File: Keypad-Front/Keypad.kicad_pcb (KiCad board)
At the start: 4 copper layers, 100.1 x 192.1 mm, 99 parts, among them J1 RTC STEMMA QT, J6 EXP QWIIC, J7 TOUCH QWIIC, U1 DS3231MZ, U2 PCA9536DP, U3 CAP1214, U4 PN5321A3HN_C1xx, U5 MCP9808_MSOP, Y3 27.12MHz

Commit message: Simplify schematic and PCB
Remove the solder jumper for SEL0/SEL1, that's been tested & is correct.

Add 0-ohm resistors for GPIO expander to accomodate future green wire hacks.

Mark the DNP components on the schematic.
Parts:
- removed JP1: SEL0, Jumper:SolderJumper-3_P1.3mm_Bridged12_Pad1.0x1.5mm
- removed JP2: SEL1, Jumper:SolderJumper-3_P1.3mm_Bridged12_Pad1.0x1.5mm
- added R31: 0, Resistor_SMD:R_0805_2012Metric_Pad1.20x1.40mm_HandSolder, B.Cu at (123.1, 181.0)
- added R32: 0, Resistor_SMD:R_0805_2012Metric_Pad1.20x1.40mm_HandSolder, B.Cu at (125.6, 181.0)
- added R33: 0, Resistor_SMD:R_0805_2012Metric_Pad1.20x1.40mm_HandSolder, B.Cu at (128.1, 181.0)
- BT1: value Battery_Cell -> CR2032
- C1, C4: value 0.1uF -> .1uF
- moved U2 0.62 mm to (123.8, 185.3)
- moved C27 0.31 mm to (124.5, 188.8)
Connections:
- U2 pad 2: GND1 -> Net-(U2-IO1)
- U2 pad 3: GND1 -> Net-(U2-IO2)
- U2 pad 5: GND1 -> Net-(U2-IO3)
- U4 pad 16: /SEL0 -> +3.3V
- U4 pad 17: /SEL1 -> GND1
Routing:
- net /SEL1: track 37.3 -> 0.00 mm, vias 2 -> 0
- net /SEL0: track 30.8 -> 0.00 mm, vias 2 -> 0
- net GND1: track 2636.9 -> 2608.6 mm, vias 40 -> 41
- net Net-(U2-IO2): track 0.00 -> 7.70 mm
- net Net-(U2-IO1): track 0.00 -> 7.02 mm
- net +3.3V: track 647.7 -> 653.9 mm
- net Net-(U2-IO3): track 0.00 -> 4.08 mm
- net /LED12: track 63.4 -> 65.0 mm
- net /TOUCH_SCL: track 273.8 -> 273.3 mm
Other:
- board text added: "CSA 2023-10-25"
- board text removed: "0"
- board text removed: "1"
- board text removed: "CSA 2023-09-27"

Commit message: More schematic cleanup
* Remove silkscreen for R23/R24, which are shorted jumpers as a netlist
hack for the PCB antenna, not "real" components.

* Remove unnecessary R15 (and its traces) now that we have PCA9536 to
drive LED12.
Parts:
- removed R15: 0, Resistor_SMD:R_0805_2012Metric_Pad1.20x1.40mm_HandSolder
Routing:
- net /LED10: track 83.2 -> 65.7 mm, vias 2 -> 0
- net /LED12: track 65.0 -> 62.8 mm
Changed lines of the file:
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@@
     (attr exclude_from_pos_files)
     (net_tie_pad_groups "1, 2")
-    (fp_text reference "R23" (at 0 -2) (layer "B.SilkS")
+    (fp_text reference "R23" (at 0 -2) (layer "B.SilkS") hide
         (effects (font (size 1 1) (thickness 0.15)) (justify mirror))
     )
@@
     (attr exclude_from_pos_files)
     (net_tie_pad_groups "1, 2")
-    (fp_text reference "R24" (at 0 -2) (layer "B.SilkS")
+    (fp_text reference "R24" (at 0 -2) (layer "B.SilkS") hide
         (effects (font (size 1 1) (thickness 0.15)) (justify mirror))
     )
@@
     )
   )
-  (footprint "Resistor_SMD:R_0805_2012Metric_Pad1.20x1.40mm_HandSolder" (layer "B.Cu")
-    (at 116.5625 185 90)
-    (descr "Resistor SMD 0805 (2012 Metric), square (rectangular) end terminal, IPC_7351 nominal with elongated pad for handsoldering. (Body size source: IPC-SM-782 page 72, https://www.pcb-3d.com/wordpress/wp-content/uploads/ipc-sm-782a_amendment_1_and_2.pdf), generated with kicad-footprint-generator")
-    (tags "resistor handsolder")
-    (property "Sheetfile" "Keypad.kicad_sch")
-    (property "Sheetname" "")
-    (property "dnp" "")
-    (property "ki_description" "Resistor, small US symbol")
-    (property "ki_keywords" "r resistor")
-    (attr smd)
-    (fp_text reference "R15" (at -3.125 0 180) (layer "B.SilkS")
-        (effects (font (size 1 1) (thickness 0.15)) (justify mirror))
-    )
-    (fp_text value "0" (at 0 -1.65 90) (layer "B.Fab")
-        (effects (font (size 1 1) (thickness 0.15)) (justify mirror))
-    )
-    (fp_text user "${REFERENCE}" (at 0 0 90) (layer "B.Fab")
-        (effects (font (size 0.5 0.5) (thickness 0.08)) (justify mirror))
-    )
-    (fp_line (start -0.227064 -0.735) (end 0.227064 -0.735)
-      (stroke (width 0.12) (type solid)) (layer "B.SilkS"))
-    (fp_line (start -0.227064 0.735) (end 0.227064 0.735)
-      (stroke (width 0.12) (type solid)) (layer "B.SilkS"))
-    (fp_line (start -1.85 -0.95) (end -1.85 0.95)
-      (stroke (width 0.05) (type solid)) (layer "B.CrtYd"))
-    (fp_line (start -1.85 0.95) (end 1.85 0.95)
-      (stroke (width 0.05) (type solid)) (layer "B.CrtYd"))
-    (fp_line (start 1.85 -0.95) (end -1.85 -0.95)
-      (stroke (width 0.05) (type solid)) (layer "B.CrtYd"))
-    (fp_line (start 1.85 0.95) (end 1.85 -0.95)
-      (stroke (width 0.05) (type solid)) (layer "B.CrtYd"))
-    (fp_line (start -1 -0.625) (end -1 0.625)
-      (stroke (width 0.1) (type solid)) (layer "B.Fab"))
-    (fp_line (start -1 0.625) (end 1 0.625)
-      (stroke (width 0.1) (type solid)) (layer "B.Fab"))
-    (fp_line (start 1 -0.625) (end -1 -0.625)
-      (stroke (width 0.1) (type solid)) (layer "B.Fab"))
-    (fp_line (start 1 0.625) (end 1 -0.625)
-      (stroke (width 0.1) (type solid)) (layer "B.Fab"))
-    (pad "1" smd roundrect (at -1 0 90) (size 1.2 1.4) (layers "B.Cu" "B.Paste" "B.Mask") (roundrect_rratio 0.2083333333)
-      (net 33 "/LED10") (pintype "passive"))
-    (pad "2" smd roundrect (at 1 0 90) (size 1.2 1.4) (layers "B.Cu" "B.Paste" "B.Mask") (roundrect_rratio 0.2083333333)
-      (net 58 "/LED12") (pintype "passive"))
-    (model "${KICAD6_3DMODEL_DIR}/Resistor_SMD.3dshapes/R_0805_2012Metric.wrl"
-      (offset (xyz 0 0 0))
-      (scale (xyz 1 1 1))
-      (rotate (xyz 0 0 0))
-    )
-  )
   (footprint "Resistor_SMD:R_1206_3216Metric_Pad1.30x1.75mm_HandSolder" (layer "B.Cu")
     (at 92.1875 77.8125)
@@
   (segment (start 149.04375 139.35625) (end 146.875 137.1875) (width 0.4) (layer "B.Cu") (net 32))
   (segment (start 149.2 176.425) (end 149.2 139.5125) (width 0.2) (layer "B.Cu") (net 32))
-  (via (at 109.212899 190.939824) (size 0.7) (drill 0.3) (layers "F.Cu" "B.Cu") (net 33))
-  (via (at 116.25 190.9375) (size 0.7) (drill 0.3) (layers "F.Cu" "B.Cu") (net 33))
-  (segment (start 109.212899 190.939824) (end 110.440223 189.7125) (width 0.15) (layer "In1.Cu") (net 33))
-  (segment (start 110.440223 189.7125) (end 115.025 189.7125) (width 0.15) (layer "In1.Cu") (net 33))
-  (segment (start 115.025 189.7125) (end 116.25 190.9375) (width 0.15) (layer "In1.Cu") (net 33))
-  (segment (start 97.1875 189.375) (end 99.375 191.5625) (width 0.15) (layer "B.Cu") (net 33))
-  (segment (start 108.590223 191.5625) (end 109.212899 190.939824) (width 0.15) (layer "B.Cu") (net 33))
-  (segment (start 116.5625 186) (end 116.5625 190.625) (width 0.15) (layer "B.Cu") (net 33))
-  (segment (start 74.6875 189.375) (end 97.1875 189.375) (width 0.15) (layer "B.Cu") (net 33))
-  (segment (start 105.3125 190.74816) (end 105.3125 191.5625) (width 0.15) (layer "B.Cu") (net 33))
+  (segment (start 106.931757 189.128903) (end 105.2068 190.85386) (width 0.15) (layer "B.Cu") (net 33))
   (segment (start 68.75 161.875) (end 67.1875 163.4375) (width 0.4) (layer "B.Cu") (net 33))
-  (segment (start 106.931757 189.128903) (end 105.3125 190.74816) (width 0.15) (layer "B.Cu") (net 33))
-  (segment (start 67.1875 181.875) (end 74.6875 189.375) (width 0.15) (layer "B.Cu") (net 33))
-  (segment (start 116.5625 190.625) (end 116.25 190.9375) (width 0.15) (layer "B.Cu") (net 33))
-  (segment (start 99.375 191.5625) (end 105.3125 191.5625) (width 0.15) (layer "B.Cu") (net 33))
+  (segment (start 105.2068 190.85386) (end 105.2068 191.3128) (width 0.15) (layer "B.Cu") (net 33))
+  (segment (start 105.2068 191.3128) (end 104.9571 191.5625) (width 0.15) (layer "B.Cu") (net 33))
+  (segment (start 97.1875 189.375) (end 74.6875 189.375) (width 0.15) (layer "B.Cu") (net 33))
+  (segment (start 74.6875 189.375) (end 67.1875 181.875) (width 0.15) (layer "B.Cu") (net 33))
   (segment (start 67.1875 163.4375) (end 67.1875 181.875) (width 0.2) (layer "B.Cu") (net 33))
-  (segment (start 105.3125 191.5625) (end 108.590223 191.5625) (width 0.15) (layer "B.Cu") (net 33))
+  (segment (start 99.375 191.5625) (end 97.1875 189.375) (width 0.15) (layer "B.Cu") (net 33))
+  (segment (start 104.9571 191.5625) (end 99.375 191.5625) (width 0.15) (layer "B.Cu") (net 33))
   (segment (start 109.787899 190.699327) (end 109.451072 190.3625) (width 0.15) (layer "B.Cu") (net 34))
   (segment (start 66.6 183.475) (end 72.8125 189.6875) (width 0.15) (layer "B.Cu") (net 34))
@@
   (segment (start 120 181.875) (end 116.875 181.875) (width 0.15) (layer "In1.Cu") (net 58))
   (segment (start 121.6 186.2875) (end 120.35 186.2875) (width 0.15) (layer "B.Cu") (net 58))
-  (segment (start 116.875 181.875) (end 116.5625 182.1875) (width 0.15) (layer "B.Cu") (net 58))
-  (segment (start 116.5625 182.1875) (end 116.5625 184) (width 0.15) (layer "B.Cu") (net 58))
   (segment (start 148.8 175.8) (end 148.8 164.425) (width 0.2) (layer "B.Cu") (net 58))
   (segment (start 119.075 185.0125) (end 119.075 182.8) (width 0.15) (layer "B.Cu") (net 58))

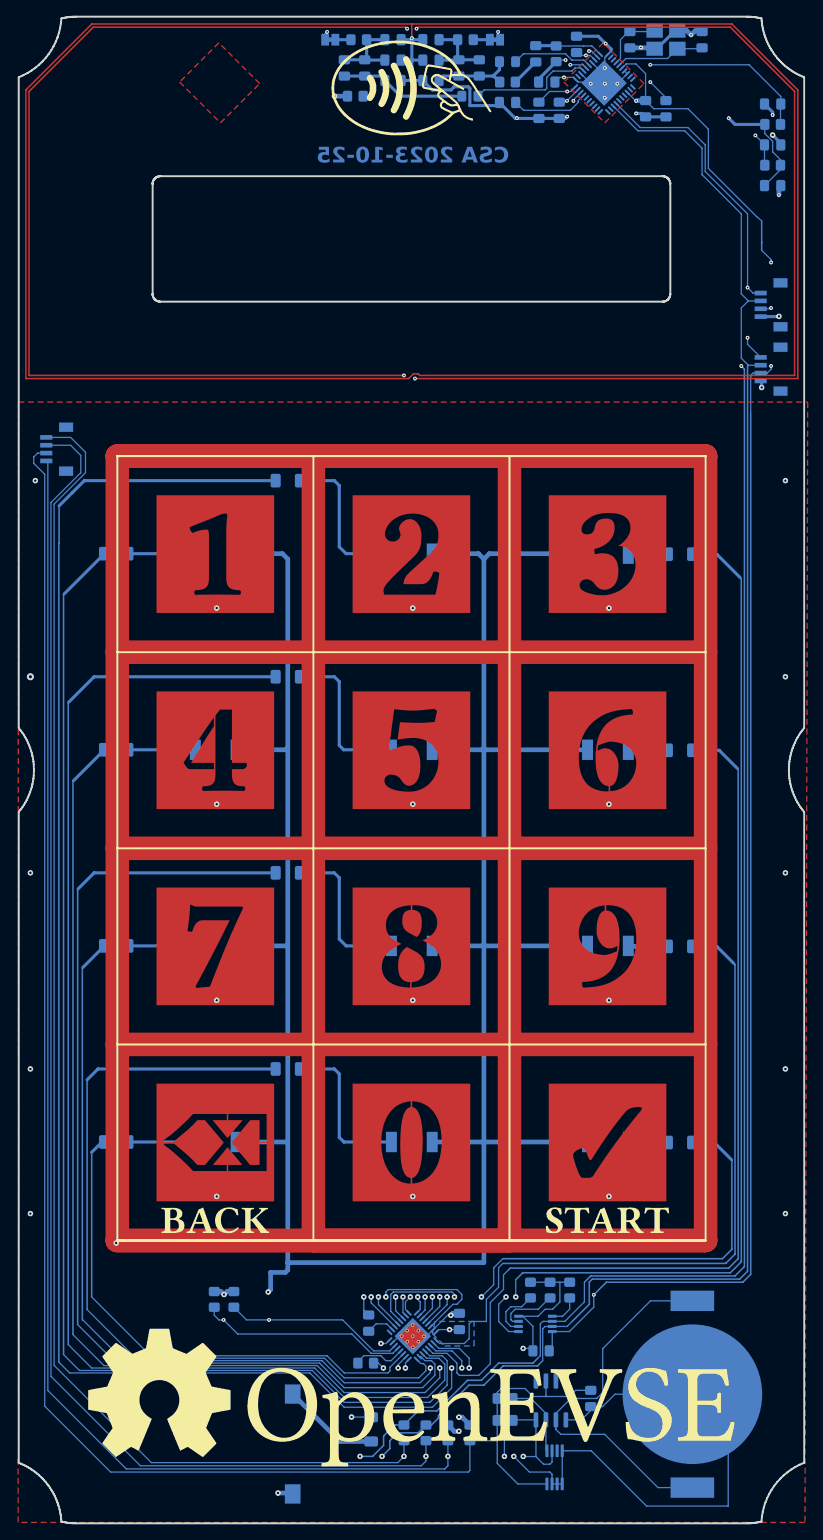
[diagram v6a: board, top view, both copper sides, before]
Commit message: More work on schematic and gerbers; fill out BOM with JLCPCB part #s
Also updated the README a bit.
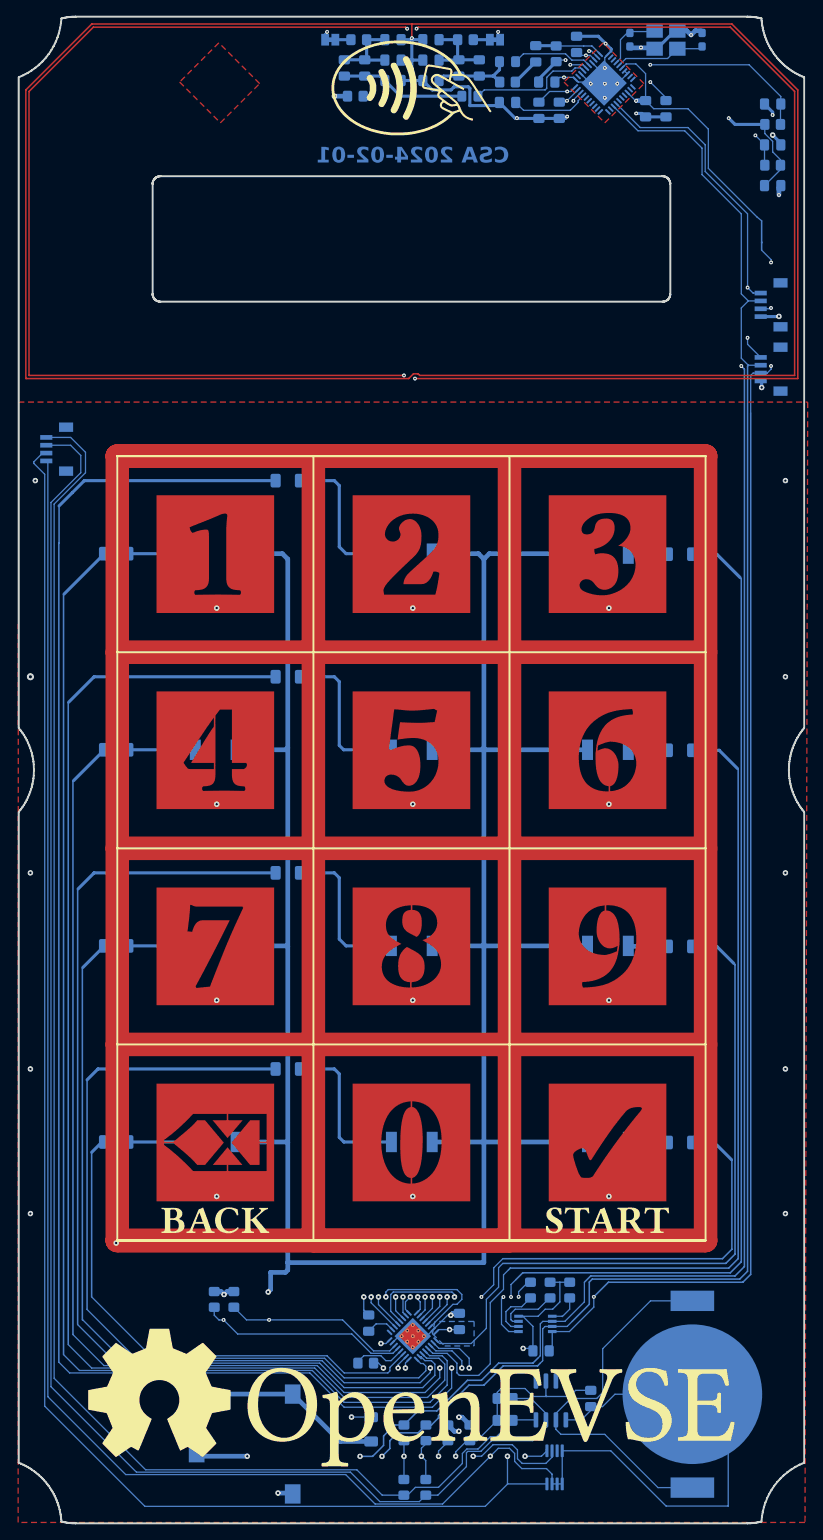
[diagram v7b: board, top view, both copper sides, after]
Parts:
- added BZ1: FUET-9650B-3V, Keypad:FUET-9650B-3V, B.Cu at (80.6, 197.9)
- added R26: 0, Resistor_SMD:R_0805_2012Metric_Pad1.20x1.40mm_HandSolder, B.Cu at (109.8, 206.1)
- added R27: 0, Resistor_SMD:R_0805_2012Metric_Pad1.20x1.40mm_HandSolder, B.Cu at (107.0, 206.1)
- BZ2: renamed from BZ1; value Buzzer -> PUI SMT-1220-TW-R
- C3: renamed from C2; footprint Capacitor_SMD:C_0805_2012Metric_Pad1.18x1.45mm_HandSolder -> Capacitor_SMD:C_0603_1608Metric_Pad1.08x0.95mm_HandSolder
- C4: renamed from C3; footprint Capacitor_SMD:C_0805_2012Metric_Pad1.18x1.45mm_HandSolder -> Capacitor_SMD:C_0603_1608Metric_Pad1.08x0.95mm_HandSolder
- D1, D10, D11, D12, D2, D3, D4, D5, D6, D7, D8, D9: value LED -> SunLED XZVG45WT-9
- FB1, FB2: value FerriteBead_Small -> Laird MI0805J102R-10
- R22: renamed from R26; value 1.0k -> 1k
- R28: renamed from R31; value 0 -> 1k
- R29: renamed from R32; value 0 -> 1k
- R30: renamed from R33; value 0 -> 1k
- renumbered C5 to C1, C14 to C10, C7 to C11, C26 to C12, C9 to C14, C25 to C15, C27 to C16, C12 to C17, C16 to C18, C17 to C19, C4 to C2, C18 to C20, C19 to C21, C20 to C22, C21 to C23, C22 to C24, C1 to C25, C23 to C26, C24 to C27, C10 to C5, C11 to C6, C8 to C7, C15 to C8, C6 to C9, J6 to J1, J7 to J2, J1 to J3, R27 to R1, R11 to R10, R2 to R11, R4 to R12, R6 to R13, R8 to R14, R10 to R15, R12 to R16, R16 to R17, R19 to R18, R17 to R19, R28 to R2, R18 to R20, R20 to R21, R25 to R23, R13 to R24, R14 to R25, R29 to R3, R21 to R31, R22 to R32, R23 to R33, R24 to R34, R30 to R4, R1 to R5, R3 to R6, R5 to R7, R7 to R8, TP14 to TP1, TP3 to TP10, TP12 to TP11, TP9 to TP12, TP10 to TP13, TP4 to TP2, TP7 to TP3, TP6 to TP4, TP1 to TP5, TP5 to TP6, TP8 to TP7, TP11 to TP8, TP2 to TP9, U3 to U1, U4 to U2, U5 to U3, U2 to U4, U1 to U5, Y3 to Y1
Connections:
- R1 pad 2: /RTC_SCL -> /TEMP_SCL
- R2 pad 2: /RTC_SDA -> /TEMP_SDA
- R28 pad 2: GND1 -> +3.3V
- U3 pad 1: /RTC_SDA -> /TEMP_SDA
- U3 pad 2: /RTC_SCL -> /TEMP_SCL
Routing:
- net /TEMP_SCL: track 0.00 -> 30.9 mm, vias 0 -> 2
- net /TEMP_SDA: track 0.00 -> 23.8 mm, vias 0 -> 2
- net GND2: track 256.7 -> 269.7 mm
- net /FEEDBACK: track 12.5 -> 24.9 mm
- net +5V: track 219.9 -> 232.1 mm, vias 0 -> 2
- net /RTC_SCL: track 205.4 -> 198.0 mm, vias 2 -> 0
- net GND1: track 2608.6 -> 2613.9 mm, vias 41 -> 42
- net +3.3V: track 653.9 -> 658.0 mm, vias 11 -> 12
- net /RTC_SDA: track 207.4 -> 206.1 mm, vias 2 -> 0
- net /LED12: track 62.8 -> 62.0 mm
- net /LED9: track 90.6 -> 90.0 mm
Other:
- board text added: "CSA 2024-02-01"
- board text removed: "CSA 2023-10-25"

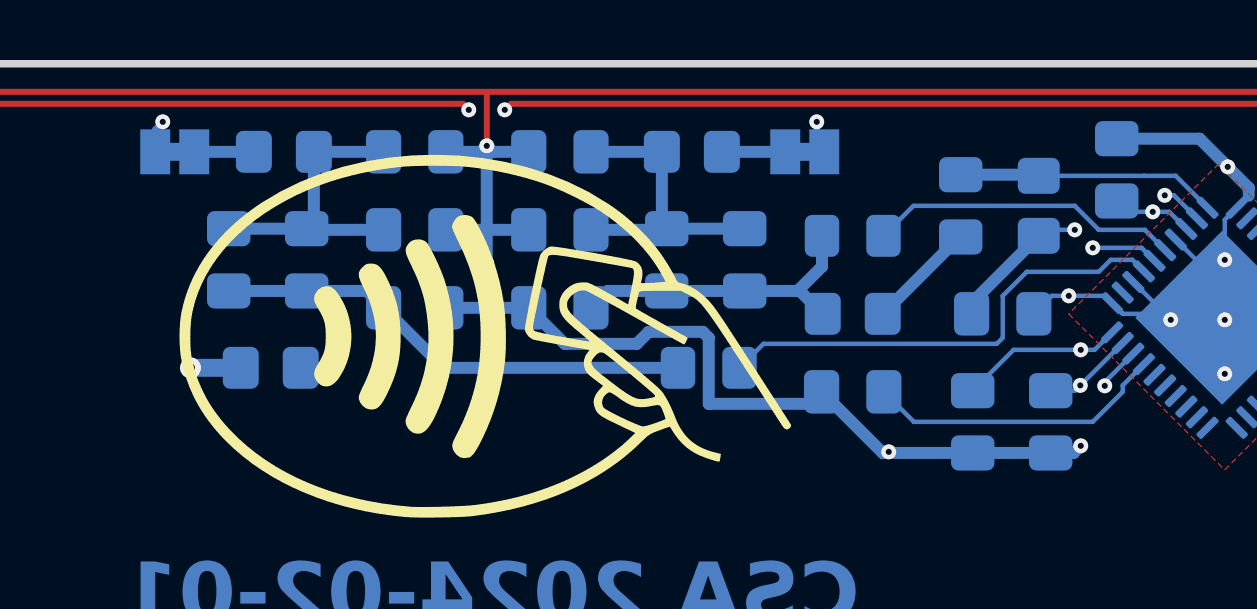
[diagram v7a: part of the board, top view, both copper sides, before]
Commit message: RFID tuning
Tuned the length of the TX1 and TX2 traces to maintain symmetry; moved
L1/L2 around a bit to the same end.  Added a zero-ohm resistor so we
can disconnect the antenna "virtual ground" from the actual ground,
as recommended by the AN1445 app note.
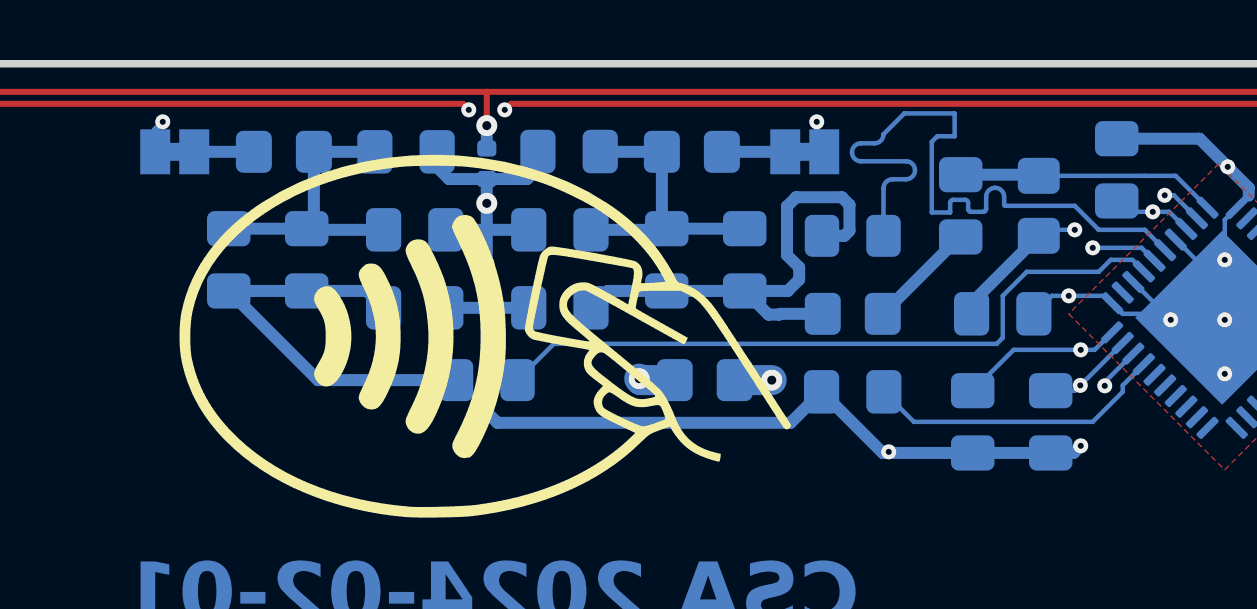
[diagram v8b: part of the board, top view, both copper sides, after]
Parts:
- added R35: 0, Resistor_SMD:R_0402_1005Metric, B.Cu at (108.0, 22.0)
- moved R21 14.5 mm to (115.3, 29.2)
- moved L1 7.41 mm to (108.0, 29.2)
- moved C27 0.31 mm to (110.7, 21.6)
- moved C26 0.29 mm to (105.3, 21.6)
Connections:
- net Net-(C17-Pad2) renamed /FEED_P
- net Net-(C19-Pad2) renamed /FEED_N
- net Net-(U2-TX1) renamed /TX_P
- net Net-(U2-TX2) renamed /TX_N
- R33 pad 1: GND1 -> Net-(R33-Pad1)
- R34 pad 2: GND1 -> Net-(R33-Pad1)
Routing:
- net Net-(R33-Pad1): track 0.00 -> 579.8 mm, vias 0 -> 7
- net GND1: track 2613.9 -> 2035.3 mm, vias 42 -> 36
- net +3.3V: track 658.0 -> 642.3 mm
- net Net-(U2-~{RSTPD}): track 28.5 -> 14.2 mm
- net /TX_N: track 10.4 -> 23.5 mm
- net /TX_P: track 16.0 -> 23.5 mm
- net /FEED_N: track 10.4 -> 17.0 mm
- net /FEED_P: track 16.0 -> 14.8 mm
